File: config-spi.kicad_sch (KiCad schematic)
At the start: 32 parts, among them J3001 PinHeader_2x7_P2mm_SMD_Shroud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, Q3001 BSS138PW, Q3002 BSS138PW, Q3003 BSS138PW, SW3001 SW_KMR211NGLFS_SMD, SW3002 CVS-03B, U3001 S25FL128SAGNFI000, U3002 XC7K160T-FFG676, U3003 TPD4E05U06QDQARQ1

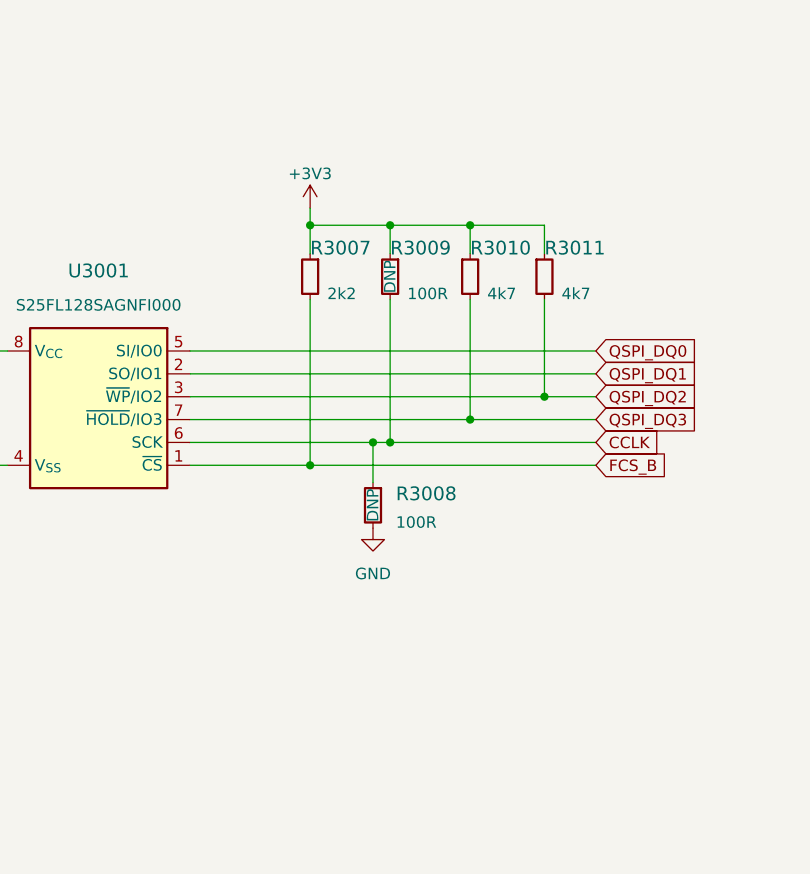
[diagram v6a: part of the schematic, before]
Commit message: Improve QSPI termination, improve power I2C WiP
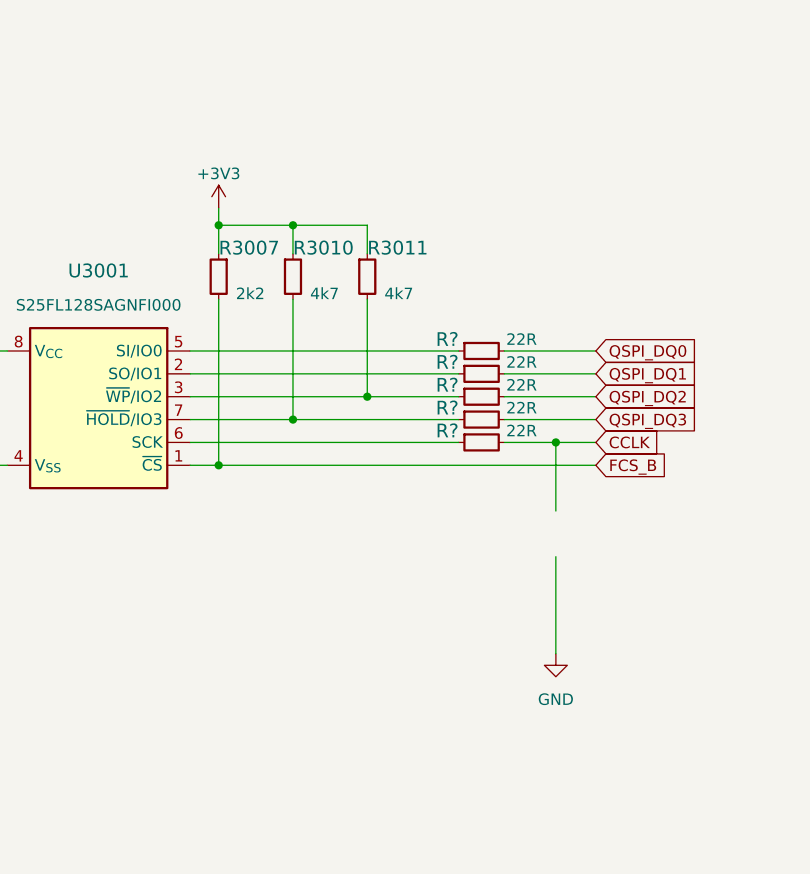
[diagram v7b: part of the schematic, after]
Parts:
- removed R3008, R3009: R_100R_0402, sodimm-ddr5-tester-footprints:R_0402_1005Metric, symbol sodimm-ddr5-tester:R_100R_0402
- added R? (x5): R_22R_0402, sodimm-ddr5-tester-footprints:R_0402_1005Metric, symbol sodimm-ddr5-tester:R_22R_0402
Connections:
- net CCLK: now also R?.2; no longer U3001.6 (SCK)
- net QSPI_DQ0: now also R?.2; no longer U3001.5 (SI/IO0)
- net QSPI_DQ1: now also R?.2; no longer U3001.2 (SO/IO1)
- net QSPI_DQ2: now also R?.2; no longer R3011.2, U3001.3 (~{WP}/IO2)
- net QSPI_DQ3: now also R?.2; no longer R3010.2, U3001.7 (~{HOLD}/IO3)
- new net: R?.1, U3001.2 (SO/IO1)
- new net: R3011.2, R?.1, U3001.3 (~{WP}/IO2)
- new net: R?.1, U3001.5 (SI/IO0)
- new net: R?.1, U3001.6 (SCK)
- new net: R3010.2, R?.1, U3001.7 (~{HOLD}/IO3)
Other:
- moved on the sheet: R3007, R3010, R3011

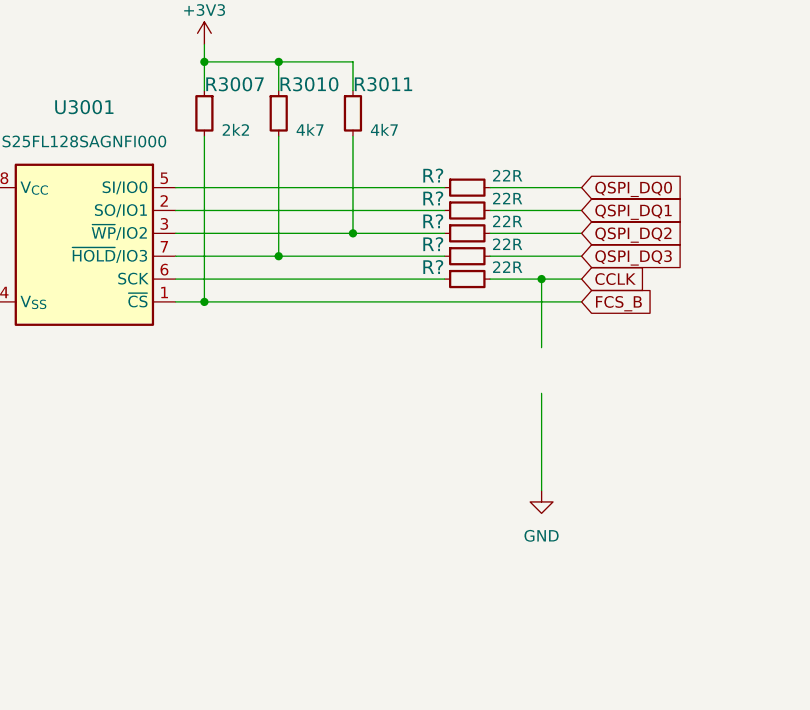
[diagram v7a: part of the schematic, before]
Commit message: Finish reworking power I2C and SPI termination
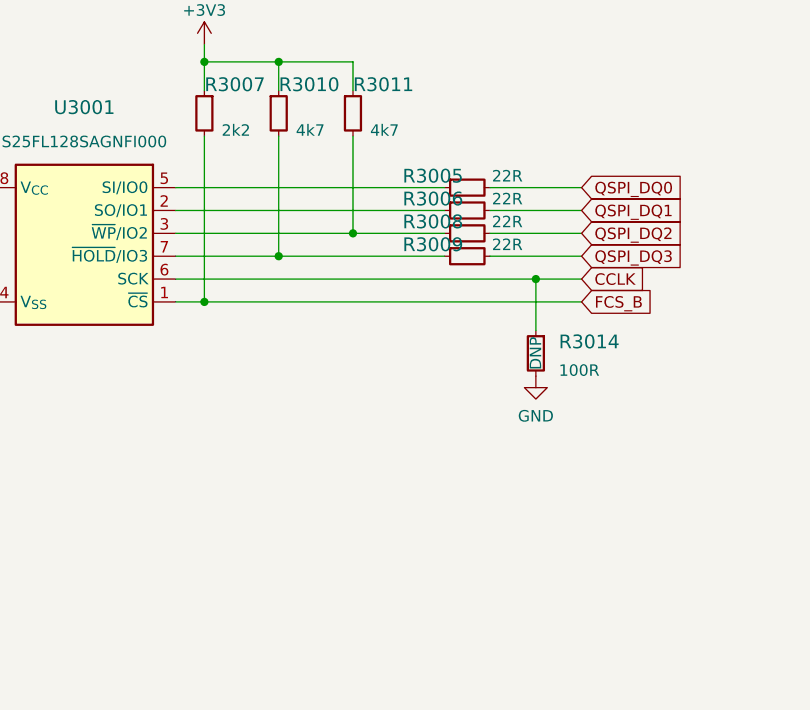
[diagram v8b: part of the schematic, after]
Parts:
- removed R?: R_22R_0402, sodimm-ddr5-tester-footprints:R_0402_1005Metric, symbol sodimm-ddr5-tester:R_22R_0402
- added R3014: R_100R_0402, sodimm-ddr5-tester-footprints:R_0402_1005Metric, symbol sodimm-ddr5-tester:R_100R_0402
- gave numbers to parts that had none: 4
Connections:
- net CCLK: now also U3001.6 (SCK), R3014.1
- net GND: now also R3014.2
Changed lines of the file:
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@@
   (junction (at 324.485 111.76) (diameter 0) (color 0 0 0 0)
   )
+  (junction (at 137.795 113.03) (diameter 0) (color 0 0 0 0)
+  )
   (junction (at 36.83 237.49) (diameter 0) (color 0 0 0 0)
   )
   (junction (at 36.83 242.57) (diameter 0) (color 0 0 0 0)
   )
-  (junction (at 138.43 113.03) (diameter 0) (color 0 0 0 0)
-  )
   (junction (at 252.73 105.41) (diameter 0) (color 0 0 0 0)
   )
@@
     (stroke (width 0) (type default) (color 0 0 0 0))
   )
-  (wire (pts (xy 138.43 113.03) (xy 138.43 120.65))
-    (stroke (width 0) (type default) (color 0 0 0 0))
-  )
   (wire (pts (xy 97.79 102.87) (xy 127.635 102.87))
     (stroke (width 0) (type default) (color 0 0 0 0))
@@
     (stroke (width 0) (type default) (color 0 0 0 0))
   )
+  (wire (pts (xy 137.795 113.03) (xy 142.875 113.03))
+    (stroke (width 0) (type default) (color 0 0 0 0))
+  )
   (wire (pts (xy 324.104 228.854) (xy 329.184 228.854))
     (stroke (width 0) (type default) (color 0 0 0 0))
@@
     (stroke (width 0) (type default) (color 0 0 0 0))
   )
-  (wire (pts (xy 138.43 136.525) (xy 138.43 125.73))
-    (stroke (width 0) (type default) (color 0 0 0 0))
-  )
   (wire (pts (xy 327.66 78.74) (xy 327.66 83.185))
     (stroke (width 0) (type default) (color 0 0 0 0))
@@
     (stroke (width 0) (type default) (color 0 0 0 0))
   )
-  (wire (pts (xy 97.79 113.03) (xy 127.635 113.03))
-    (stroke (width 0) (type default) (color 0 0 0 0))
-  )
   (wire (pts (xy 158.75 225.425) (xy 157.48 225.425))
     (stroke (width 0) (type default) (color 0 0 0 0))
@@
     (stroke (width 0) (type default) (color 0 0 0 0))
   )
+  (wire (pts (xy 137.795 113.03) (xy 137.795 118.745))
+    (stroke (width 0) (type default) (color 0 0 0 0))
+  )
   (wire (pts (xy 284.48 85.725) (xy 284.48 87.63))
     (stroke (width 0) (type default) (color 0 0 0 0))
@@
     (stroke (width 0) (type default) (color 0 0 0 0))
   )
-  (wire (pts (xy 138.43 113.03) (xy 142.875 113.03))
+  (wire (pts (xy 97.79 113.03) (xy 137.795 113.03))
     (stroke (width 0) (type default) (color 0 0 0 0))
   )
@@
     (stroke (width 0) (type default) (color 0 0 0 0))
   )
-  (wire (pts (xy 132.715 113.03) (xy 138.43 113.03))
-    (stroke (width 0) (type default) (color 0 0 0 0))
-  )
   (wire (pts (xy 285.75 100.33) (xy 280.67 100.33))
     (stroke (width 0) (type default) (color 0 0 0 0))
@@
   (symbol (lib_id "sodimm-ddr5-tester:R_22R_0402") (at 127.635 102.87 0) (unit 1)
     (in_bom yes) (on_board yes)
-    (property "Reference" "R?" (id 0) (at 126.365 101.6 0)
+    (property "Reference" "R3005" (id 0) (at 126.365 101.6 0)
       (effects (font (size 1.524 1.524)))
     )
@@
     (pin "1")
   )
-  (symbol (lib_id "sodimm-ddr5-tester:R_22R_0402") (at 127.635 113.03 0) (unit 1)
+  (symbol (lib_id "sodimm-ddr5-tester:R_100R_0402") (at 137.795 118.745 270) (unit 1)
     (in_bom yes) (on_board yes)
-    (property "Reference" "R?" (id 0) (at 126.365 111.76 0)
-      (effects (font (size 1.524 1.524)))
+    (property "Reference" "R3014" (id 0) (at 140.335 120.015 90)
+      (effects (font (size 1.524 1.524)) (justify left))
     )
-    (property "Value" "R_22R_0402" (id 1) (at 147.955 125.73 0)
+    (property "Value" "R_100R_0402" (id 1) (at 125.095 139.065 0)
       (effects (font (size 1.27 1.27) (thickness 0.15)) (justify left bottom) hide)
     )
-    (property "Footprint" "sodimm-ddr5-tester-footprints:R_0402_1005Metric" (id 2) (at 147.955 128.27 0)
+    (property "Footprint" "sodimm-ddr5-tester-footprints:R_0402_1005Metric" (id 2) (at 122.555 139.065 0)
       (effects (font (size 1.27 1.27) (thickness 0.15)) (justify left bottom) hide)
     )
-    (property "Datasheet" "https://www.bourns.com/docs/product-datasheets/cr.pdf" (id 3) (at 147.955 130.81 0)
+    (property "Datasheet" "https://www.bourns.com/docs/product-datasheets/cr.pdf" (id 3) (at 120.015 139.065 0)
       (effects (font (size 1.27 1.27) (thickness 0.15)) (justify left bottom) hide)
     )
-    (property "Manufacturer" "Bourns" (id 4) (at 147.955 135.89 0)
+    (property "Manufacturer" "Bourns" (id 4) (at 114.935 139.065 0)
       (effects (font (size 1.27 1.27) (thickness 0.15)) (justify left bottom) hide)
     )
-    (property "MPN" "CR0402-FX-22R0GLF" (id 5) (at 147.955 133.35 0)
+    (property "MPN" "CR0402-FX-1000GLF" (id 5) (at 117.475 139.065 0)
       (effects (font (size 1.27 1.27) (thickness 0.15)) (justify left bottom) hide)
     )
-    (property "Val" "22R" (id 6) (at 134.62 111.76 0)
-      (effects (font (size 1.27 1.27) (thickness 0.15)))
+    (property "Val" "100R" (id 6) (at 140.335 123.1899 90)
+      (effects (font (size 1.27 1.27) (thickness 0.15)) (justify left))
     )
-    (property "License" "Apache-2.0" (id 7) (at 147.955 138.43 0)
+    (property "License" "Apache-2.0" (id 7) (at 112.395 139.065 0)
       (effects (font (size 1.27 1.27) (thickness 0.15)) (justify left bottom) hide)
     )
-    (property "Author" "Antmicro" (id 8) (at 147.955 140.97 0)
+    (property "Author" "Antmicro" (id 8) (at 109.855 139.065 0)
       (effects (font (size 1.27 1.27) (thickness 0.15)) (justify left bottom) hide)
     )
-    (property "Tolerance" "1%" (id 9) (at 147.955 123.19 0)
+    (property "Tolerance" "1%" (id 9) (at 127.635 139.065 0)
       (effects (font (size 1.27 1.27)) (justify left bottom) hide)
     )
+    (property "DNP" "DNP" (id 10) (at 137.795 121.285 0))
     (pin "1")
     (pin "2")
   )
-  (symbol (lib_id "sodimm-ddr5-tester:GND") (at 138.43 136.525 0) (unit 1)
-    (in_bom yes) (on_board yes) (fields_autoplaced)
-    (property "Reference" "#PWR?" (id 0) (at 138.43 142.875 0)
-      (effects (font (size 1.27 1.27)) hide)
-    )
-    (property "Value" "GND" (id 1) (at 138.43 141.605 0))
-    (property "Footprint" "" (id 2) (at 138.43 136.525 0)
-      (effects (font (size 1.27 1.27)) hide)
-    )
-    (property "Datasheet" "" (id 3) (at 138.43 136.525 0)
-      (effects (font (size 1.27 1.27)) hide)
-    )
-    (property "Author" "Antmicro" (id 4) (at 147.32 144.145 0)
-      (effects (font (size 1.27 1.27) (thickness 0.15)) (justify left bottom) hide)
-    )
-    (property "License" "Apache-2.0" (id 5) (at 147.32 146.685 0)
-      (effects (font (size 1.27 1.27) (thickness 0.15)) (justify left bottom) hide)
-    )
-    (pin "1")
-  )
   (symbol (lib_id "sodimm-ddr5-tester:R_22R_0402") (at 127.635 110.49 0) (unit 1)
     (in_bom yes) (on_board yes)
-    (property "Reference" "R?" (id 0) (at 126.365 109.22 0)
+    (property "Reference" "R3009" (id 0) (at 126.365 109.22 0)
       (effects (font (size 1.524 1.524)))
     )
@@
   (symbol (lib_id "sodimm-ddr5-tester:R_22R_0402") (at 127.635 105.41 0) (unit 1)
     (in_bom yes) (on_board yes)
-    (property "Reference" "R?" (id 0) (at 126.365 104.14 0)
+    (property "Reference" "R3006" (id 0) (at 126.365 104.14 0)
       (effects (font (size 1.524 1.524)))
     )
@@
     (pin "1")
   )
+  (symbol (lib_id "sodimm-ddr5-tester:GND") (at 137.795 123.825 0) (unit 1)
+    (in_bom yes) (on_board yes) (fields_autoplaced)
+    (property "Reference" "#PWR0293" (id 0) (at 137.795 130.175 0)
+      (effects (font (size 1.27 1.27)) hide)
+    )
+    (property "Value" "GND" (id 1) (at 137.795 128.27 0))
+    (property "Footprint" "" (id 2) (at 137.795 123.825 0)
+      (effects (font (size 1.27 1.27)) hide)
+    )
+    (property "Datasheet" "" (id 3) (at 137.795 123.825 0)
+      (effects (font (size 1.27 1.27)) hide)
+    )
+    (property "Author" "Antmicro" (id 4) (at 146.685 131.445 0)
+      (effects (font (size 1.27 1.27) (thickness 0.15)) (justify left bottom) hide)
+    )
+    (property "License" "Apache-2.0" (id 5) (at 146.685 133.985 0)
+      (effects (font (size 1.27 1.27) (thickness 0.15)) (justify left bottom) hide)
+    )
+    (pin "1")
+  )
   (symbol (lib_id "sodimm-ddr5-tester:+3.3V") (at 243.84 245.745 0) (mirror y) (unit 1)
     (in_bom yes) (on_board yes) (fields_autoplaced)
@@
   (symbol (lib_id "sodimm-ddr5-tester:R_22R_0402") (at 127.635 107.95 0) (unit 1)
     (in_bom yes) (on_board yes)
-    (property "Reference" "R?" (id 0) (at 126.365 106.68 0)
+    (property "Reference" "R3008" (id 0) (at 126.365 106.68 0)
       (effects (font (size 1.524 1.524)))
     )
